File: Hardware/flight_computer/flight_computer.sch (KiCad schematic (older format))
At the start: 4 parts

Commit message: Updates stm to connectors
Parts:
- removed C?: C_0u1, Capacitors_SMD:C_0805, symbol openDrone_parts:C_0u1
- removed R?: 470R, symbol Device:R
- removed U?: FRAM_128K, Housings_SOIC:SOIC-8_3.9x4.9mm_Pitch1.27mm, symbol openDrone_parts:FRAM_128K
- added C? (x6): C_0u1, Capacitors_SMD:C_0805, symbol openDrone_parts:C_0u1
- added C? (x2): C_8p, Capacitors_SMD:C_0805, symbol openDrone_parts:C_8p
- added C? (x4): C_2u2, Capacitors_SMD:C_0805, symbol openDrone_parts:C_2u2
- added U?: FRAM_128K, Housings_SOIC:SOIC-8_3.9x4.9mm_Pitch1.27mm, symbol openDrone_parts:FRAM_128K
- added Y?: Crystal_24MHZ, drone_footprints:NX3225SA-24.000M-STD-CSR-1, symbol openDrone_parts:Crystal_24MHZ
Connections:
- net labels added: FMU_CH1, FMU_CH2, FMU_CH3, FMU_CH4, FMU_UART7_RX, FMU_UART7_TX, FMU_USART2_CTS, FMU_USART2_RTS, FMU_USART2_RX, FMU_USART2_TX, FMU_USART8_RX, FMU_USART8_TX, FMU_VBAT, FMU_VDD_3V3, FRAM_CS, RSSI_IN
- net labels removed: ALARM, BATT_CURRENT_SENS, BATT_VOLTAGE_SENS, CAN2_RX, CAN2_TX, EXTERN_CS, EXTERN_DRDY, FMU-I2C1_SCL, FMU-I2C1_SDA, FMU-I2C2_SCL, FMU-I2C2_SDA, FMU-SWO, FMU-VDD_3V3, FMU_UART4_RX, FMU_UART_TX, IO_USART1_TX, SWCLK, SWDIO, VBUS, VDD_5V_PERIPH_EN, VDD_5V_SENS, VDD_BACKUP_VALID, VDD_BRICK_VALID, ~FRAM_CS
- wire segments 48 -> 126
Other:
- moved on the sheet: U?

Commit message: Adds sensors
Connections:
- net labels added: IMU_ACCEL_CS, IMU_MISO, IMU_MOSI, IMU_SCK, VDD_3V3_SENSORS_EN
- net labels removed: 5V, VCC
- wire segments 126 -> 123

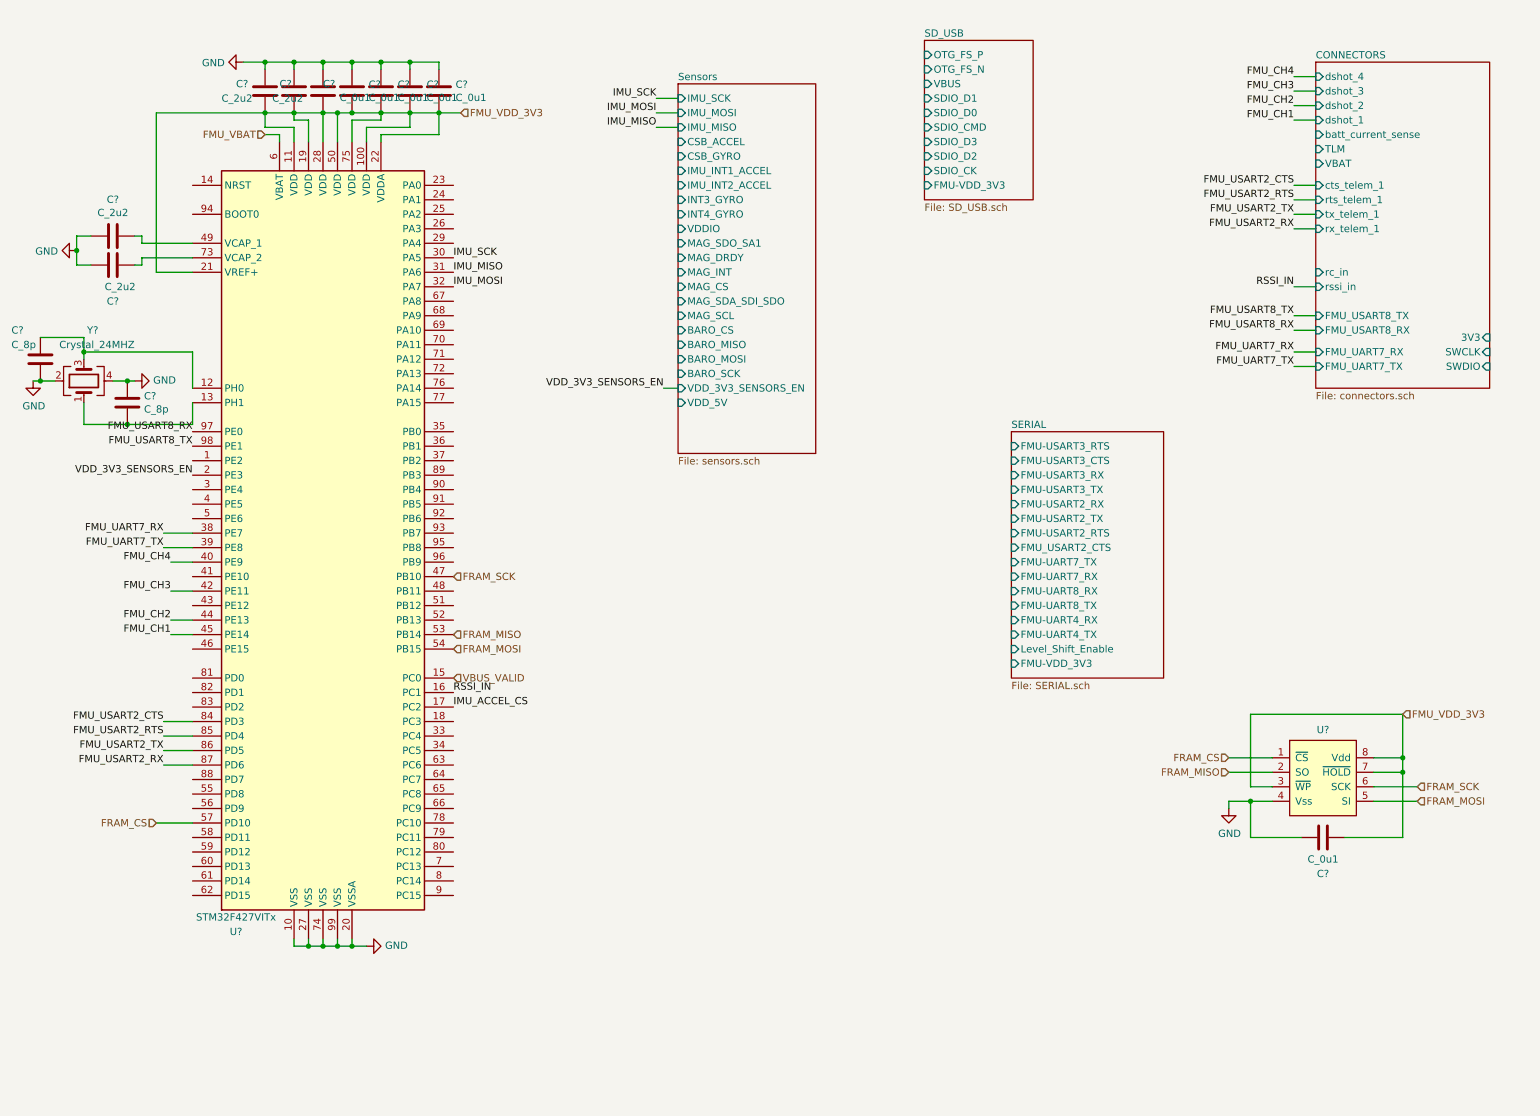
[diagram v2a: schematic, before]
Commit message: Adds more sensor connections and communication with stm
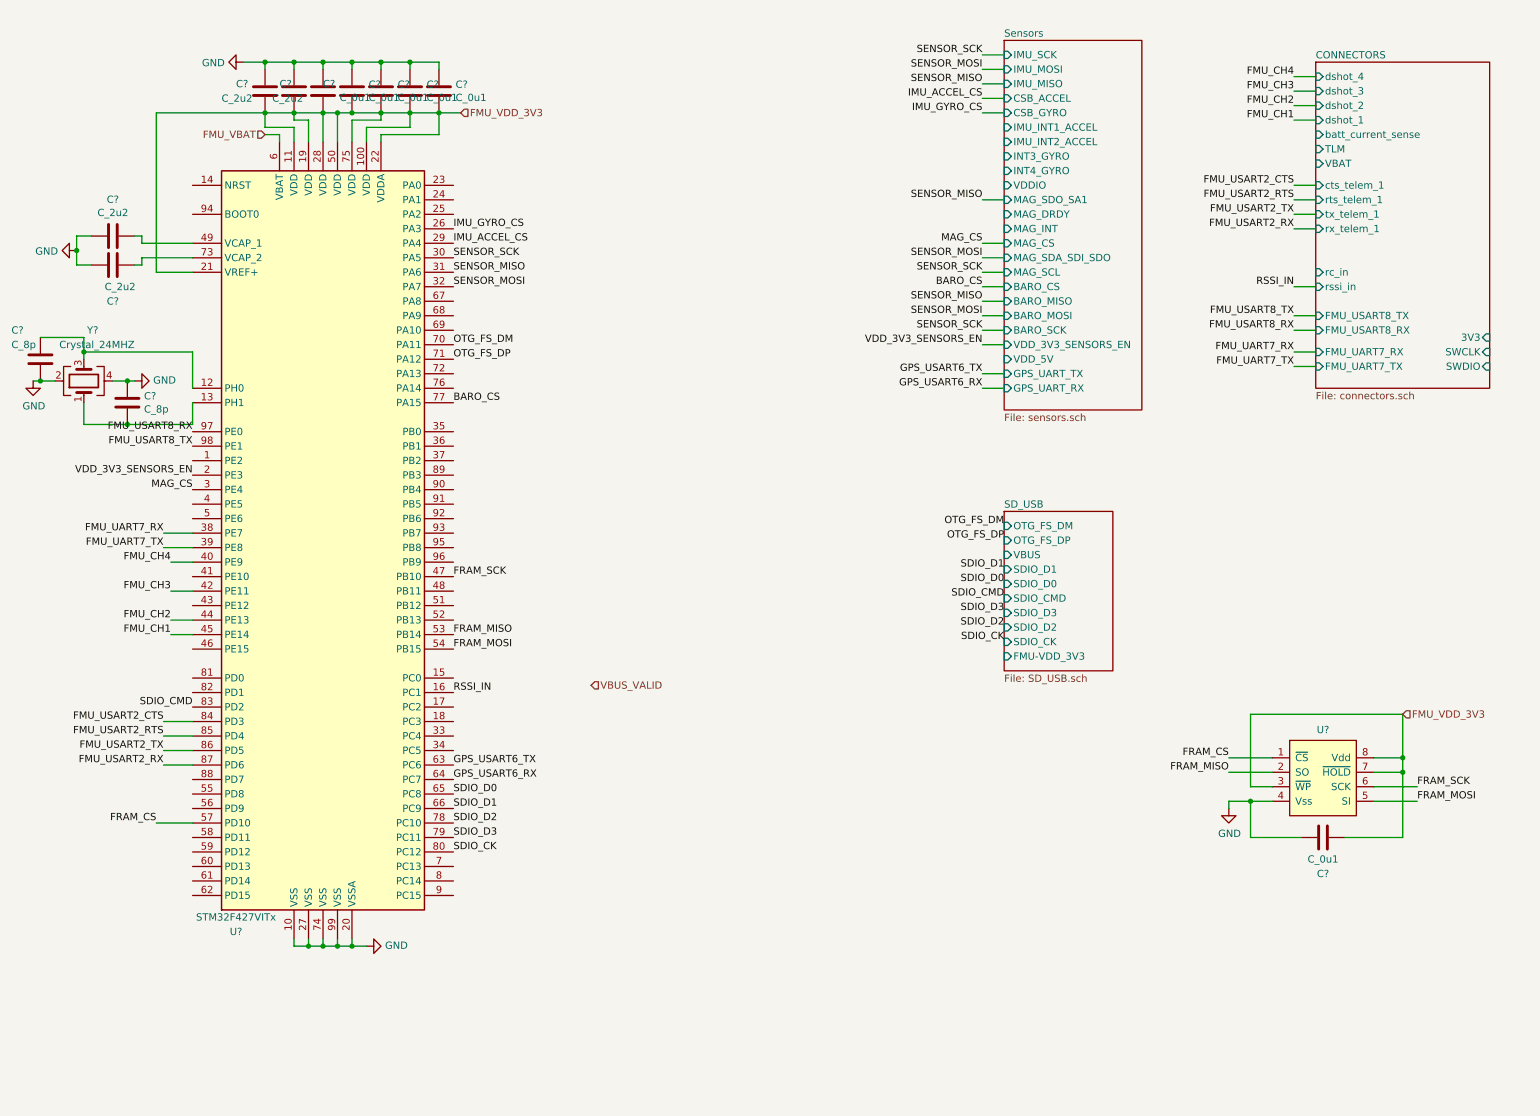
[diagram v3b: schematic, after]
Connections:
- net IMU_ACCEL_CS: now also U?.29 (PA4); no longer U?.17 (PC2)
- net VBUS_VALID: no longer U?.15 (PC0)
- net IMU_GYRO_CS: now reaches U?.26 (PA3)
- net MAG_CS: now reaches U?.3 (PE4)
- net GPS_USART6_TX: now reaches U?.63 (PC6)
- net GPS_USART6_RX: now reaches U?.64 (PC7)
- net SDIO_D0: now reaches U?.65 (PC8)
- net SDIO_D1: now reaches U?.66 (PC9)
- net OTG_FS_DM: now reaches U?.70 (PA11)
- net OTG_FS_DP: now reaches U?.71 (PA12)
- net BARO_CS: now reaches U?.77 (PA15)
- net SDIO_D2: now reaches U?.78 (PC10)
- net SDIO_D3: now reaches U?.79 (PC11)
- net SDIO_CK: now reaches U?.80 (PC12)
- net SDIO_CMD: now reaches U?.83 (PD2)
- net IMU_MISO renamed SENSOR_MISO
- net IMU_MOSI renamed SENSOR_MOSI
- net IMU_SCK renamed SENSOR_SCK
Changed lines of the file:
@@
 $Descr A4 11693 8268
 encoding utf-8
-Sheet 1 5
+Sheet 1 4
 Title ""
 Date ""
@@
 $EndDescr
 $Sheet
-S 5300 950  950  2550
+S 7550 650  950  2550
 U 5F5F0393
 F0 "Sensors" 50
 F1 "sensors.sch" 50
-F2 "IMU_SCK" I L 5300 1050 50
-F3 "IMU_MOSI" I L 5300 1150 50
-F4 "IMU_MISO" I L 5300 1250 50
-F5 "CSB_ACCEL" I L 5300 1350 50
-F6 "CSB_GYRO" I L 5300 1450 50
-F7 "IMU_INT1_ACCEL" I L 5300 1550 50
-F8 "IMU_INT2_ACCEL" I L 5300 1650 50
-F9 "INT3_GYRO" I L 5300 1750 50
-F10 "INT4_GYRO" I L 5300 1850 50
-F11 "VDDIO" I L 5300 1950 50
-F12 "MAG_SDO_SA1" I L 5300 2050 50
-F13 "MAG_DRDY" I L 5300 2150 50
-F14 "MAG_INT" I L 5300 2250 50
-F15 "MAG_CS" I L 5300 2350 50
-F16 "MAG_SDA_SDI_SDO" I L 5300 2450 50
-F17 "MAG_SCL" I L 5300 2550 50
-F18 "BARO_CS" I L 5300 2650 50
-F19 "BARO_MISO" I L 5300 2750 50
-F20 "BARO_MOSI" I L 5300 2850 50
-F21 "BARO_SCK" I L 5300 2950 50
-F22 "VDD_3V3_SENSORS_EN" I L 5300 3050 50
-F23 "VDD_5V" I L 5300 3150 50
+F2 "IMU_SCK" I L 7550 750 50
+F3 "IMU_MOSI" I L 7550 850 50
+F4 "IMU_MISO" I L 7550 950 50
+F5 "CSB_ACCEL" I L 7550 1050 50
+F6 "CSB_GYRO" I L 7550 1150 50
+F7 "IMU_INT1_ACCEL" I L 7550 1250 50
+F8 "IMU_INT2_ACCEL" I L 7550 1350 50
+F9 "INT3_GYRO" I L 7550 1450 50
+F10 "INT4_GYRO" I L 7550 1550 50
+F11 "VDDIO" I L 7550 1650 50
+F12 "MAG_SDO_SA1" I L 7550 1750 50
+F13 "MAG_DRDY" I L 7550 1850 50
+F14 "MAG_INT" I L 7550 1950 50
+F15 "MAG_CS" I L 7550 2050 50
+F16 "MAG_SDA_SDI_SDO" I L 7550 2150 50
+F17 "MAG_SCL" I L 7550 2250 50
+F18 "BARO_CS" I L 7550 2350 50
+F19 "BARO_MISO" I L 7550 2450 50
+F20 "BARO_MOSI" I L 7550 2550 50
+F21 "BARO_SCK" I L 7550 2650 50
+F22 "VDD_3V3_SENSORS_EN" I L 7550 2750 50
+F23 "VDD_5V" I L 7550 2850 50
+F24 "GPS_UART_TX" I L 7550 2950 50
+F25 "GPS_UART_RX" I L 7550 3050 50
 $EndSheet
 $Sheet
-S 7600 3350 1050 1700
-U 5F615E1F
-F0 "SERIAL" 50
-F1 "SERIAL.sch" 50
-F2 "FMU-USART3_RTS" I L 7600 3450 50
-F3 "FMU-USART3_CTS" I L 7600 3550 50
-F4 "FMU-USART3_RX" I L 7600 3650 50
-F5 "FMU-USART3_TX" I L 7600 3750 50
-F6 "FMU-USART2_RX" I L 7600 3850 50
-F7 "FMU-USART2_TX" I L 7600 3950 50
-F8 "FMU-USART2_RTS" I L 7600 4050 50
-F9 "FMU_USART2_CTS" I L 7600 4150 50
-F10 "FMU-UART7_TX" I L 7600 4250 50
-F11 "FMU-UART7_RX" I L 7600 4350 50
-F12 "FMU-UART8_RX" I L 7600 4450 50
-F13 "FMU-UART8_TX" I L 7600 4550 50
-F14 "FMU-UART4_RX" I L 7600 4650 50
-F15 "Level_Shift_Enable" I L 7600 4850 50
-F16 "FMU-VDD_3V3" I L 7600 4950 50
-F17 "FMU-UART4_TX" I L 7600 4750 50
-$EndSheet
-$Sheet
-S 7000 650  750  1100
+S 7550 3900 750  1100
 U 5F615F42
 F0 "SD_USB" 50
 F1 "SD_USB.sch" 50
-F2 "OTG_FS_P" I L 7000 750 50
-F3 "OTG_FS_N" I L 7000 850 50
-F4 "VBUS" I L 7000 950 50
-F5 "SDIO_D1" I L 7000 1050 50
-F6 "SDIO_D0" I L 7000 1150 50
-F7 "SDIO_CMD" I L 7000 1250 50
-F8 "SDIO_D3" I L 7000 1350 50
-F9 "SDIO_D2" I L 7000 1450 50
-F10 "SDIO_CK" I L 7000 1550 50
-F11 "FMU-VDD_3V3" I L 7000 1650 50
+F2 "VBUS" I L 7550 4200 50
+F3 "SDIO_D1" I L 7550 4300 50
+F4 "SDIO_D0" I L 7550 4400 50
+F5 "SDIO_CMD" I L 7550 4500 50
+F6 "SDIO_D3" I L 7550 4600 50
+F7 "SDIO_D2" I L 7550 4700 50
+F8 "SDIO_CK" I L 7550 4800 50
+F9 "FMU-VDD_3V3" I L 7550 4900 50
+F10 "OTG_FS_DM" I L 7550 4000 50
+F11 "OTG_FS_DP" I L 7550 4100 50
 $EndSheet
-Text HLabel 3750 5050 2    50   Input ~ 0
+Text HLabel 4700 5100 2    50   Input ~ 0
 VBUS_VALID
 $Comp
@@
 	1    0    0    -1
 $EndComp
-Text HLabel 10400 5900 2    50   Input ~ 0
-FRAM_MOSI
-Text HLabel 10400 5800 2    50   Input ~ 0
-FRAM_SCK
-Text HLabel 9100 5600 0    50   Input ~ 0
-FRAM_CS
-Text HLabel 9100 5700 0    50   Input ~ 0
-FRAM_MISO
 $Comp
 L openDrone_parts:C_0u1 C?
@@
 Wire Wire Line
 	10300 5700 10300 6150
-Text HLabel 1700 6050 0    50   Input ~ 0
-FRAM_CS
-Text HLabel 3750 4750 2    50   Input ~ 0
-FRAM_MISO
-Text HLabel 3750 4350 2    50   Input ~ 0
-FRAM_SCK
-Text HLabel 3750 4850 2    50   Input ~ 0
-FRAM_MOSI
 Wire Wire Line
 	1700 6050 1950 6050
@@
 	9700 2350 9550 2350
 Text Label 3750 2150 0    50   ~ 0
-IMU_SCK
+SENSOR_SCK
 Text Label 3750 2250 0    50   ~ 0
-IMU_MISO
+SENSOR_MISO
 Text Label 3750 2350 0    50   ~ 0
-IMU_MOSI
-Text Label 3750 5250 0    50   ~ 0
+SENSOR_MOSI
+Text Label 3750 2050 0    50   ~ 0
 IMU_ACCEL_CS
-Text Label 5150 1050 2    50   ~ 0
-IMU_SCK
-Text Label 5150 1250 2    50   ~ 0
-IMU_MISO
-Text Label 5150 1150 2    50   ~ 0
-IMU_MOSI
-Wire Wire Line
-	5150 1050 5300 1050
-Wire Wire Line
-	5300 1150 5150 1150
-Wire Wire Line
-	5150 1250 5300 1250
+Wire Wire Line
+	7400 750  7550 750
+Wire Wire Line
+	7550 850  7400 850
+Wire Wire Line
+	7400 950  7550 950
 Text Label 1950 3650 2    50   ~ 0
 VDD_3V3_SENSORS_EN
-Text Label 5200 3050 2    50   ~ 0
+Text Label 7400 2750 2    50   ~ 0
 VDD_3V3_SENSORS_EN
-Wire Wire Line
-	5300 3050 5200 3050
 $Sheet
 S 9700 800  1200 2250
@@
 F21 "FMU_USART8_RX" I L 9700 2650 50
 $EndSheet
+Text Label 7400 1050 2    50   ~ 0
+IMU_ACCEL_CS
+Wire Wire Line
+	7550 1050 7400 1050
+Text Label 3750 1950 0    50   ~ 0
+IMU_GYRO_CS
+Text Label 7400 1150 2    50   ~ 0
+IMU_GYRO_CS
+Wire Wire Line
+	7550 1150 7400 1150
+Text Label 3750 3150 0    50   ~ 0
+BARO_CS
+Wire Wire Line
+	7550 2350 7400 2350
+Wire Wire Line
+	7400 2450 7550 2450
+Wire Wire Line
+	7550 2550 7400 2550
+Wire Wire Line
+	7400 2650 7550 2650
+Text Label 7400 750  2    50   ~ 0
+SENSOR_SCK
+Text Label 7400 950  2    50   ~ 0
+SENSOR_MISO
+Text Label 7400 850  2    50   ~ 0
+SENSOR_MOSI
+Text Label 7400 2350 2    50   ~ 0
+BARO_CS
+Text Label 7400 2550 2    50   ~ 0
+SENSOR_MOSI
+Text Label 7400 2450 2    50   ~ 0
+SENSOR_MISO
+Text Label 7400 2650 2    50   ~ 0
+SENSOR_SCK
+Text Label 7400 2150 2    50   ~ 0
+SENSOR_MOSI
+Text Label 7400 1750 2    50   ~ 0
+SENSOR_MISO
+Text Label 7400 2250 2    50   ~ 0
+SENSOR_SCK
+Text Label 1950 3750 2    50   ~ 0
+MAG_CS
+Text Label 7400 2050 2    50   ~ 0
+MAG_CS
+Wire Wire Line
+	7400 1750 7550 1750
+Wire Wire Line
+	7550 2050 7400 2050
+Wire Wire Line
+	7400 2150 7550 2150
+Wire Wire Line
+	7550 2250 7400 2250
+Text Label 3750 4350 0    50   ~ 0
+FRAM_SCK
+Text Label 3750 4750 0    50   ~ 0
+FRAM_MISO
+Text Label 3750 4850 0    50   ~ 0
+FRAM_MOSI
+Text Label 1700 6050 2    50   ~ 0
+FRAM_CS
+Text Label 9100 5600 2    50   ~ 0
+FRAM_CS
+Text Label 9100 5700 2    50   ~ 0
+FRAM_MISO
+Text Label 10400 5800 0    50   ~ 0
+FRAM_SCK
+Text Label 10400 5900 0    50   ~ 0
+FRAM_MOSI
+Text Label 3750 5650 0    50   ~ 0
+GPS_USART6_TX
+Text Label 3750 5750 0    50   ~ 0
+GPS_USART6_RX
+Wire Wire Line
+	7550 2950 7400 2950
+Wire Wire Line
+	7550 3050 7400 3050
+Wire Wire Line
+	7400 2750 7550 2750
+Text Label 1950 5250 2    50   ~ 0
+SDIO_CMD
+Text Label 3750 6250 0    50   ~ 0
+SDIO_CK
+Text Label 3750 6150 0    50   ~ 0
+SDIO_D3
+Text Label 3750 6050 0    50   ~ 0
+SDIO_D2
+Text Label 3750 5950 0    50   ~ 0
+SDIO_D1
+Text Label 3750 5850 0    50   ~ 0
+SDIO_D0
+Text Label 7400 2950 2    50   ~ 0
+GPS_USART6_TX
+Text Label 7400 3050 2    50   ~ 0
+GPS_USART6_RX
+Text Label 7550 4400 2    50   ~ 0
+SDIO_D0
+Text Label 7550 4300 2    50   ~ 0
+SDIO_D1
+Text Label 7550 4700 2    50   ~ 0
+SDIO_D2
+Text Label 7550 4600 2    50   ~ 0
+SDIO_D3
+Text Label 7550 4800 2    50   ~ 0
+SDIO_CK
+Text Label 7550 4500 2    50   ~ 0
+SDIO_CMD
+Text Label 3750 2750 0    50   ~ 0
+OTG_FS_DM
+Text Label 3750 2850 0    50   ~ 0
+OTG_FS_DP
+Text Label 7550 4000 2    50   ~ 0
+OTG_FS_DM
+Text Label 7550 4100 2    50   ~ 0
+OTG_FS_DP
 $EndSCHEMATC

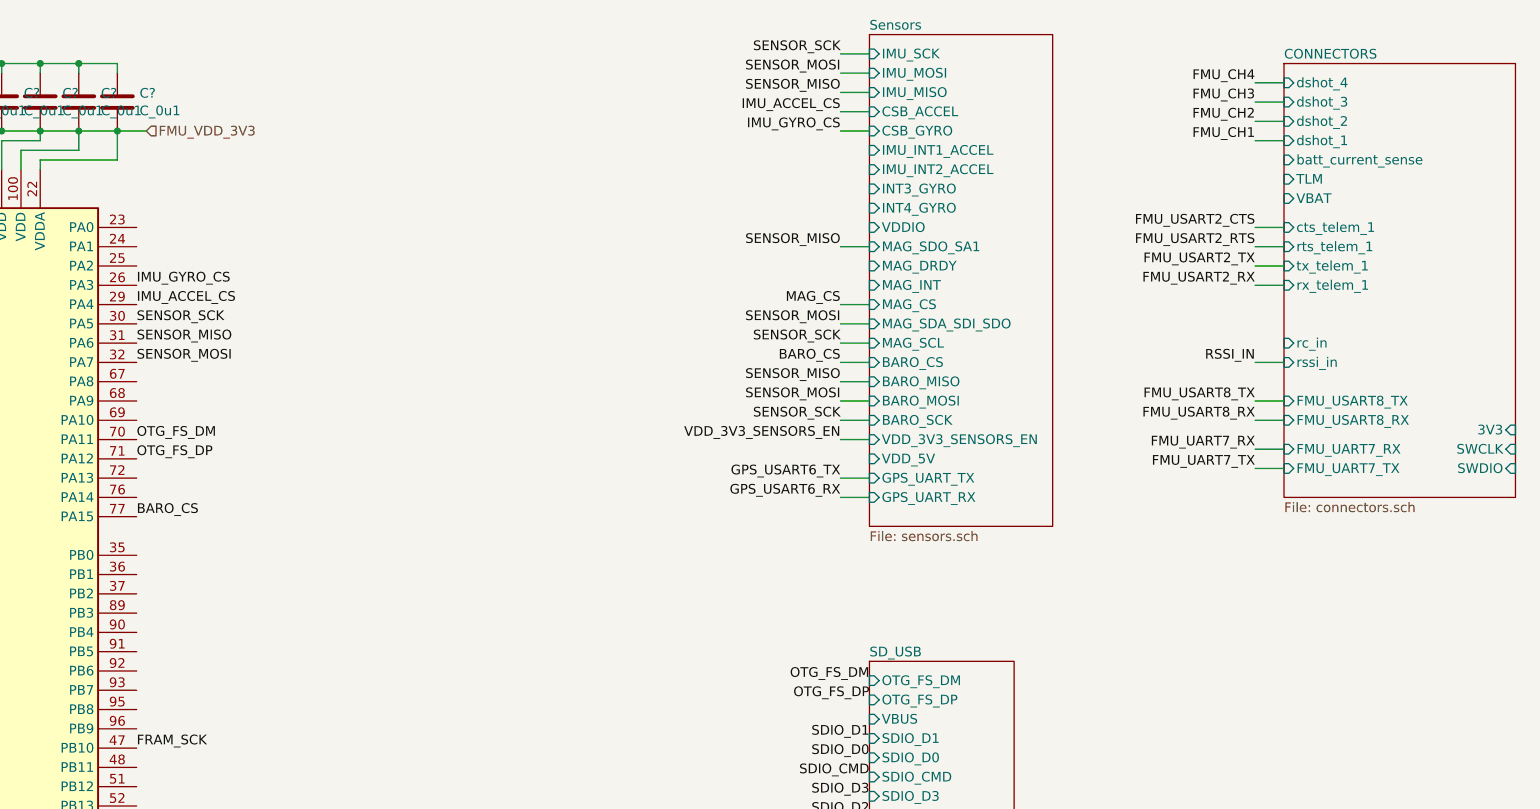
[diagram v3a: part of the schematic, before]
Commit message: Adds JTAG connections
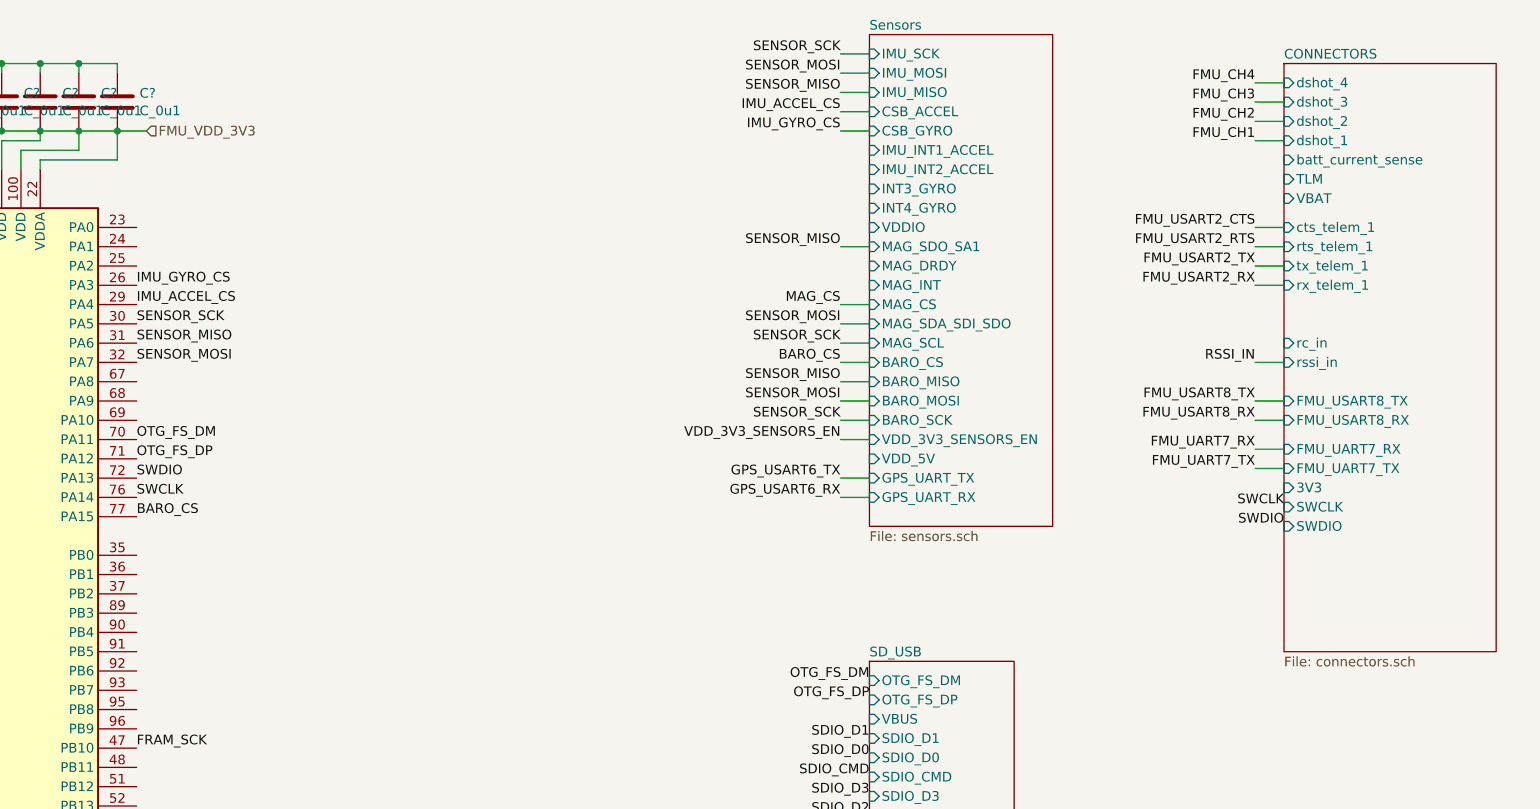
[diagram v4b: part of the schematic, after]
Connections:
- net SWDIO: now reaches U?.72 (PA13)
- net SWCLK: now reaches U?.76 (PA14)
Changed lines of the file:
@@
 VDD_3V3_SENSORS_EN
 $Sheet
-S 9700 800  1200 2250
+S 9700 800  1100 3050
 U 5F7684E9
 F0 "CONNECTORS" 50
@@
 F15 "FMU_UART7_RX" I L 9700 2800 50
 F16 "FMU_UART7_TX" I L 9700 2900 50
-F17 "SWCLK" I R 10900 2800 50
-F18 "SWDIO" I R 10900 2900 50
-F19 "3V3" I R 10900 2700 50
+F17 "SWCLK" I L 9700 3100 50
+F18 "SWDIO" I L 9700 3200 50
+F19 "3V3" I L 9700 3000 50
 F20 "FMU_USART8_TX" I L 9700 2550 50
 F21 "FMU_USART8_RX" I L 9700 2650 50
@@
 Text Label 7550 4100 2    50   ~ 0
 OTG_FS_DP
+Text Label 3750 2950 0    50   ~ 0
+SWDIO
+Text Label 3750 3050 0    50   ~ 0
+SWCLK
+Text Label 9700 3200 2    50   ~ 0
+SWDIO
+Text Label 9700 3100 2    50   ~ 0
+SWCLK
 $EndSCHEMATC
